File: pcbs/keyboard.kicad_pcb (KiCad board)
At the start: 2 copper layers, 178 x 136.4 mm, 106 parts, among them J1 Jumper, J10 Jumper, J11 Jumper, J12 Jumper, J13 Jumper, J14 Jumper, J15 Jumper, J16 Jumper, J17 Jumper, J18 Jumper, J2 Jumper, J3 Jumper, J4 Jumper, J5 Jumper, J6 Jumper, J7 Jumper, J8 Jumper, J9 Jumper

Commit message: routed pcb
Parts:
- removed the ? at (185.8, 123.2) (x2)
- removed the G*** at (187.0, 131.0)
- removed the G*** at (185.9, 131.0)
- added ? (x2): , lib:text, F.Cu at (185.8, 123.2)
- added G***: LOGO, Custom:Logo, F.Cu at (186.5, 130.8)
- added G***: LOGO, Custom:Logo, B.Cu at (185.4, 130.8)
- D1, D10, D11, D12, D13, D14, D15, D16, D17, D18, D19, D2, D20, D21, D22, D23, D24, D25, D26, D27, D28, D29, D3, D30, D31, D32, D33, D34, D4, D5, D6, D7, D8, D9: footprint ComboDiode -> ceoloide:diode_tht_sod123; moved to B.Cu
- S26, S27, S28, S29, S30, S31, S32, S33, S34: footprint MX -> ceoloide:switch_mx; moved to B.Cu
- moved D25 12.0 mm to (205.3, 187.1), turned to -122 degrees
- moved D24 12.0 mm to (189.1, 177.0), turned to -122 degrees
- moved D1 12.0 mm to (56.0, 130.9), turned to -90 degrees
- moved D10 12.0 mm to (113.2, 135.0), turned to -90 degrees
- moved D11 12.0 mm to (113.2, 116.0), turned to -90 degrees
- moved D12 12.0 mm to (113.2, 96.9), turned to -90 degrees
- moved D17 12.0 mm to (151.2, 138.0), turned to -90 degrees
- moved D18 12.0 mm to (151.2, 119.0), turned to -90 degrees
- moved D19 12.0 mm to (151.2, 99.9), turned to -90 degrees
- moved D2 12.0 mm to (56.0, 111.9), turned to -90 degrees
- moved D20 12.0 mm to (170.3, 141.0), turned to -90 degrees
- moved D21 12.0 mm to (170.3, 122.0), turned to -90 degrees
- moved D22 12.0 mm to (170.3, 102.9), turned to -90 degrees
- moved D3 12.0 mm to (75.0, 150.0), turned to -90 degrees
- moved D4 12.0 mm to (75.0, 130.9), turned to -90 degrees
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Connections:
- D12 pad 1: row2 -> row1
- D16 pad 1: row2 -> row1
- D19 pad 1: row2 -> row1
- D22 pad 1: row2 -> row1
- D27 pad 1: row2 -> row1
- D28 pad 1: row2 -> row1
- S26 pad 1: col0 -> outer2_top
- S26 pad 2: outer2_top -> col0
- S27 pad 1: col1 -> outer1_top
- S27 pad 2: outer1_top -> col1
- S28 pad 1: col2 -> pinky_top
- S28 pad 2: pinky_top -> col2
- S29 pad 1: col2 -> pinky_num
- S29 pad 2: pinky_num -> col2
- S30 pad 1: col3 -> ring_num
- S30 pad 2: ring_num -> col3
- S31 pad 1: col4 -> middle_num
- S31 pad 2: middle_num -> col4
- S32 pad 1: col5 -> index_num
- S32 pad 2: index_num -> col5
- S33 pad 1: col6 -> inner_num
- S33 pad 2: inner_num -> col6
- S34 pad 1: col1 -> home_high
- S34 pad 2: home_high -> col1
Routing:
- net col0: track 0.00 -> 363.1 mm, vias 0 -> 1
- net col1: track 0.00 -> 313.3 mm, vias 0 -> 2
- net col2: track 0.00 -> 238.2 mm, vias 0 -> 3
- net row0: track 0.00 -> 235.5 mm, vias 0 -> 8
- net row3: track 0.00 -> 205.6 mm, vias 0 -> 7
- net col3: track 0.00 -> 203.1 mm, vias 0 -> 3
- net row4: track 0.00 -> 199.5 mm, vias 0 -> 7
- net col4: track 0.00 -> 182.0 mm, vias 0 -> 4
- net col5: track 0.00 -> 168.8 mm, vias 0 -> 2
- net row2: track 0.00 -> 163.7 mm, vias 0 -> 7
- net col6: track 0.00 -> 143.2 mm, vias 0 -> 1
- net row1: track 0.00 -> 138.4 mm, vias 0 -> 7
- net GND: track 12.2 -> 149.9 mm, vias 0 -> 7
- net ENCA: track 0.00 -> 122.7 mm, vias 0 -> 3
- net ENCB: track 0.00 -> 99.3 mm, vias 0 -> 3
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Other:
- outline, holes or cut-outs redrawn

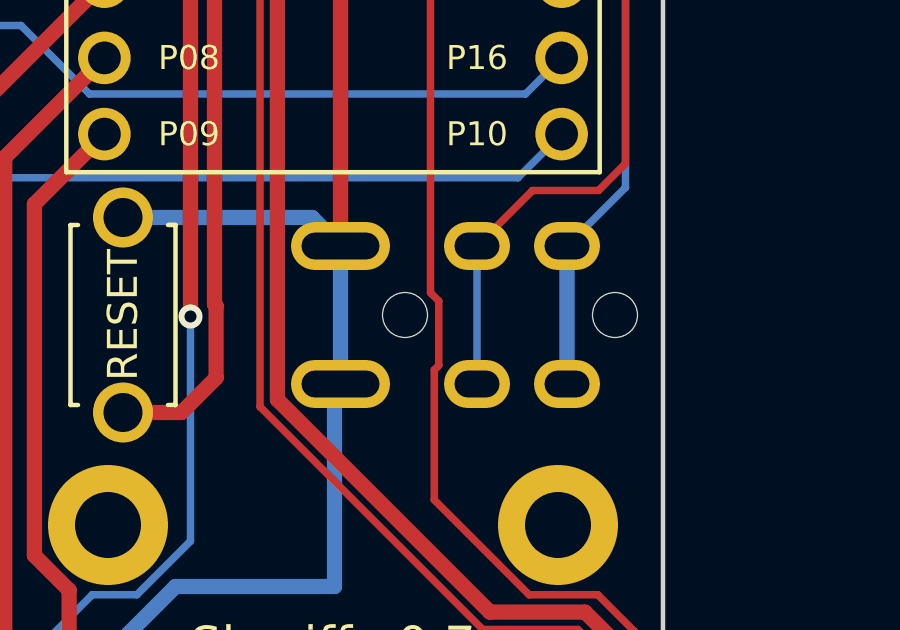
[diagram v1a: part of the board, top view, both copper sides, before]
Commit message: added teardrops
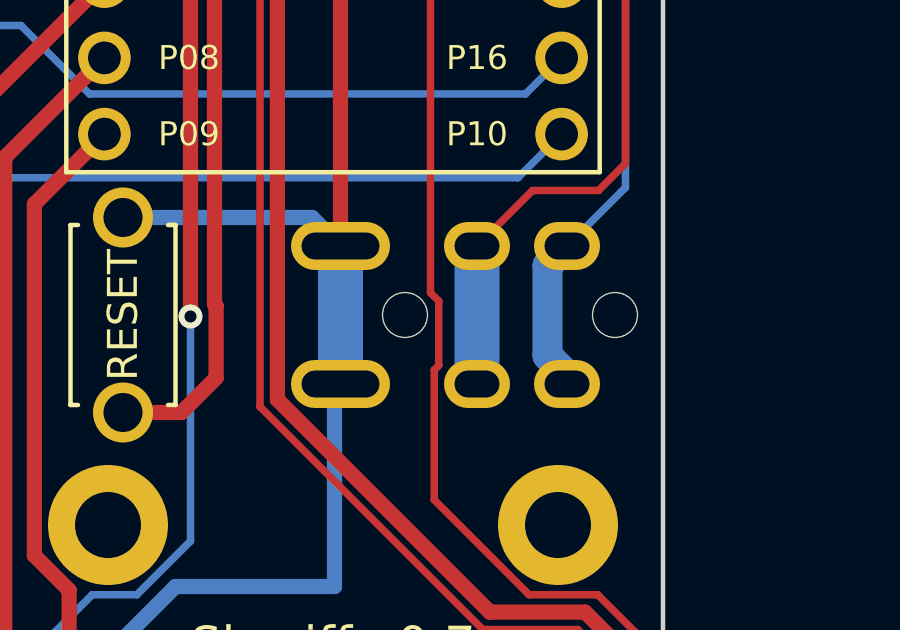
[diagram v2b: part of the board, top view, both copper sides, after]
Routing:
- net VCC: track 44.6 -> 45.1 mm

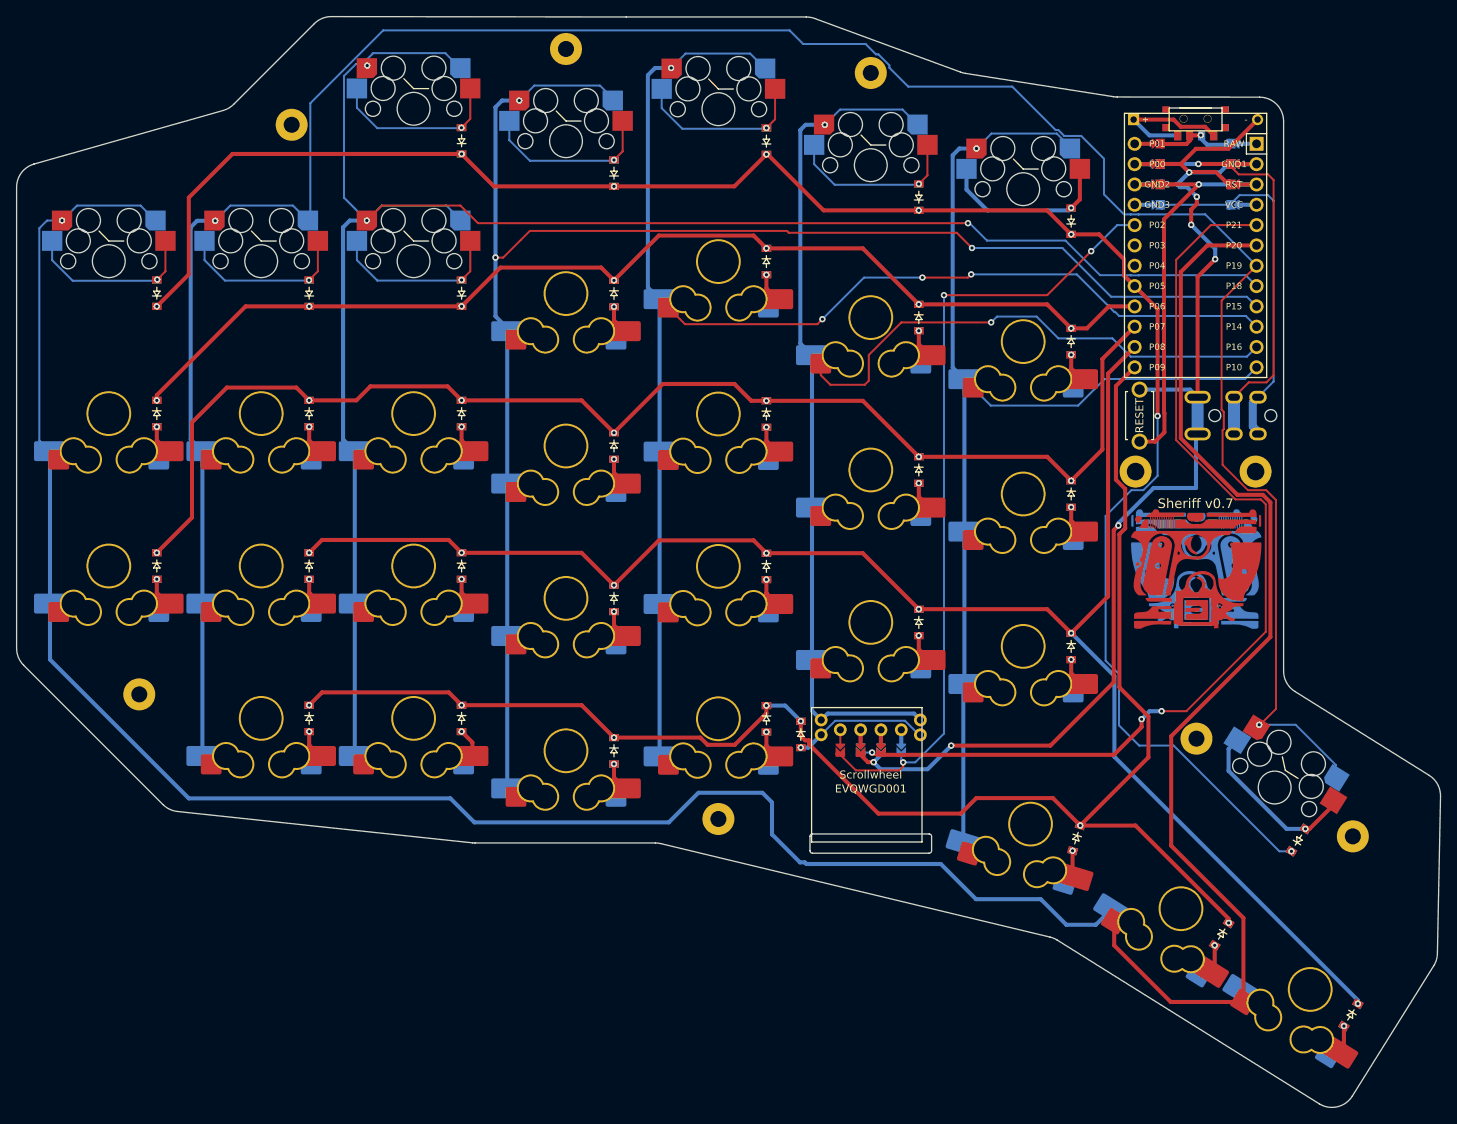
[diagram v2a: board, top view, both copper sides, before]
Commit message: fixed rotor pinout, updated jumper side
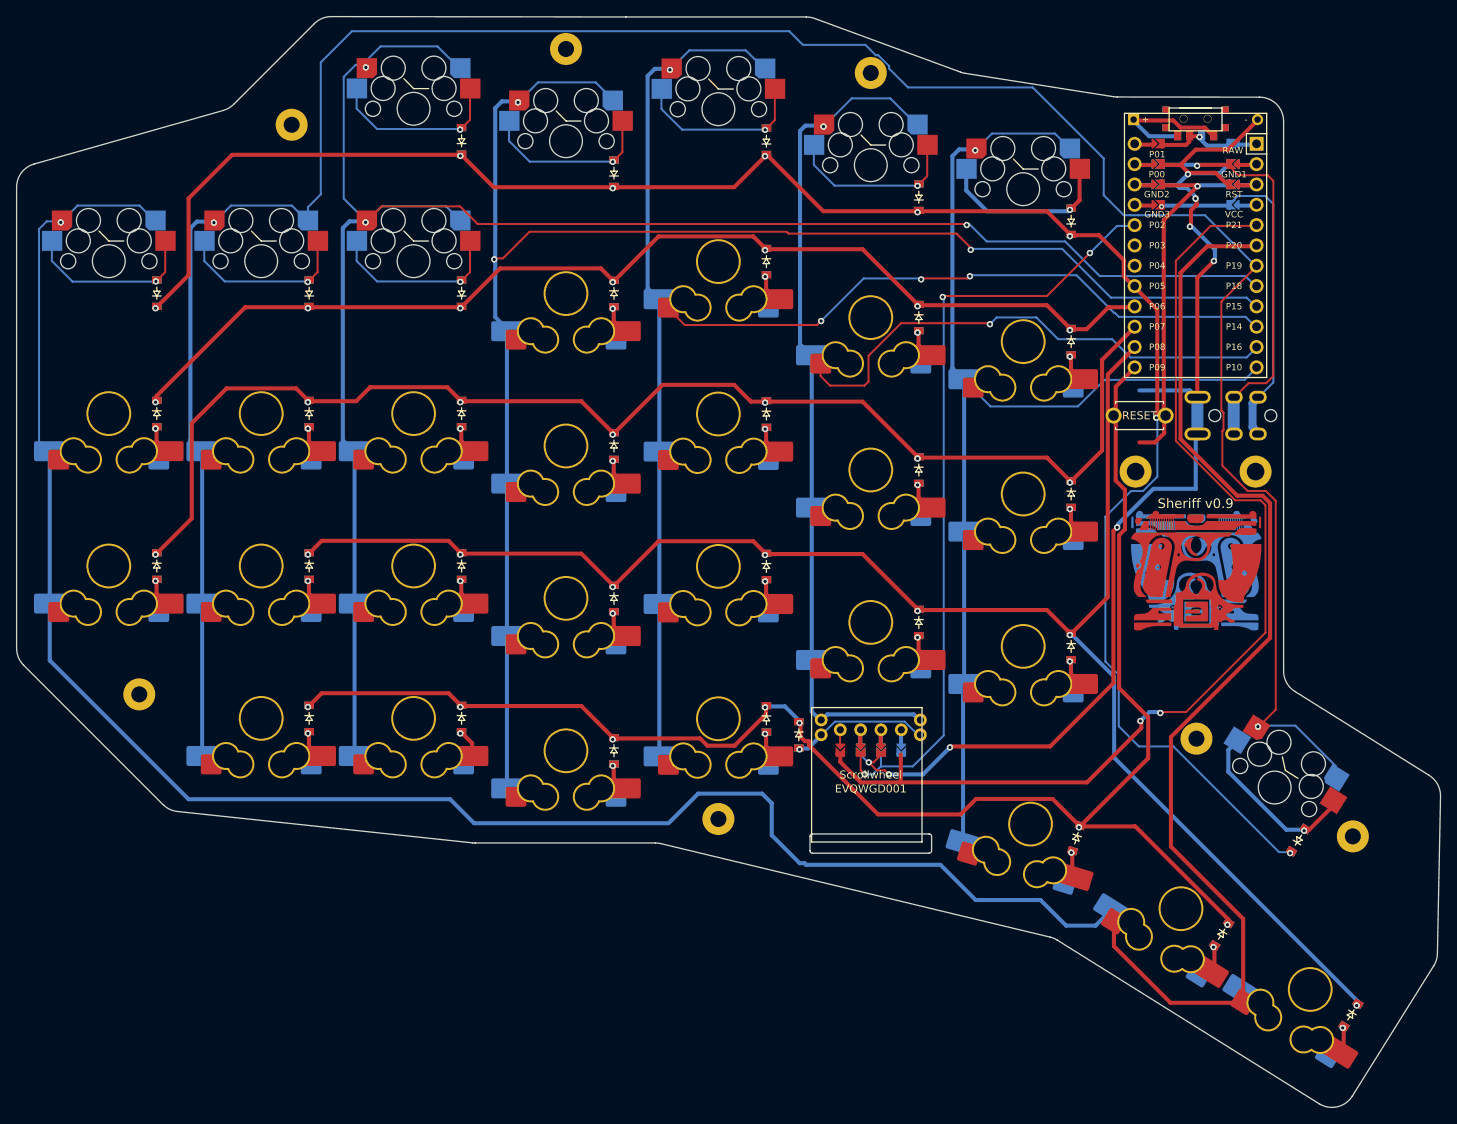
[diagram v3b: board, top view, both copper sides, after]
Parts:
- removed the ? at (185.8, 123.2) (x2)
- removed the G*** at (186.5, 130.8)
- removed the G*** at (185.4, 130.8)
- added ? (x2): , lib:text, F.Cu at (185.8, 123.2)
- added G***: LOGO, Custom:Logo, F.Cu at (186.5, 131.0)
- added G***: LOGO, Custom:Logo, B.Cu at (185.4, 131.0)
- moved D35 0.25 mm to (136.2, 152.1)
- turned _1 to 180 degrees
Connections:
- net ENCA_GND renamed GND_ENCB
- net ENCB_undef renamed ENCA_undef
- net GND_ENCA renamed ENCB_GND
- net undef_ENCB renamed undef_ENCA
- J1 pad 2: ENCB -> ENCA
- J2 pad 2: GND -> ENCB
- J3 pad 2: ENCA -> GND
- J4 pad 2: ENCB -> ENCA
- J5 pad 2: GND -> ENCB
- J6 pad 2: ENCA -> GND
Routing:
- net ENCA: track 122.7 -> 131.8 mm, vias 3 -> 2
- net col1: track 313.3 -> 316.0 mm
- net GND: track 149.9 -> 151.5 mm, vias 7 -> 8
- net col5: track 168.8 -> 170.0 mm
- net ENCB: track 99.3 -> 98.4 mm
- net col2: track 238.2 -> 239.0 mm
- net VCC: track 45.1 -> 45.0 mm, vias 0 -> 1
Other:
- outline, holes or cut-outs redrawn

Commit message: idk
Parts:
- moved D35 0.25 mm to (136.5, 152.1)
- turned _1 to -90 degrees
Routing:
- net col2: track 239.0 -> 240.4 mm
- net col1: track 316.0 -> 317.2 mm
- net row3: track 205.6 -> 206.8 mm
- net row1: track 138.4 -> 139.3 mm
- net row2: track 163.7 -> 164.5 mm
- net ENCA: track 131.8 -> 131.1 mm, vias 2 -> 3
- net row4: track 199.5 -> 200.0 mm
